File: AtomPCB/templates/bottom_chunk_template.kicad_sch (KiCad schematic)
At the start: 8 parts, among them J1 DF40HC_4.0_-40DS-0.4V_70_, U1 ATtiny416-M, U6 MPM3610AGQV-P

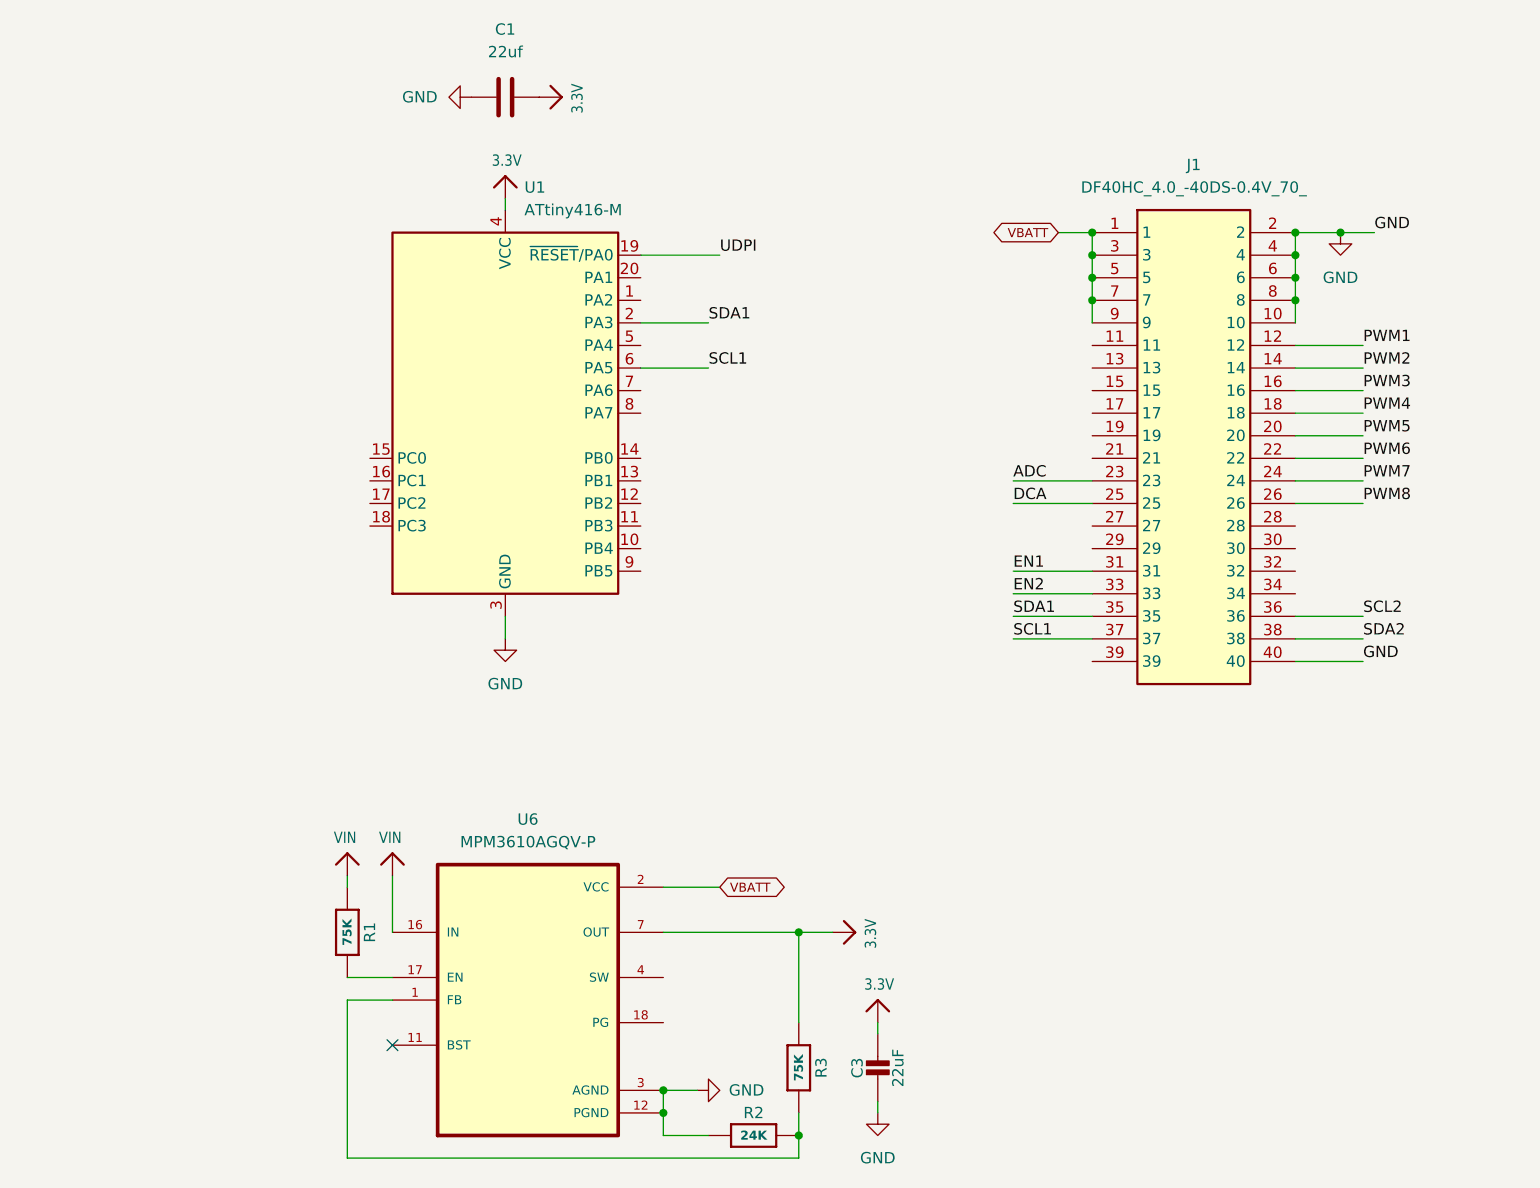
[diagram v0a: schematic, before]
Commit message: first pcb panel order placed!
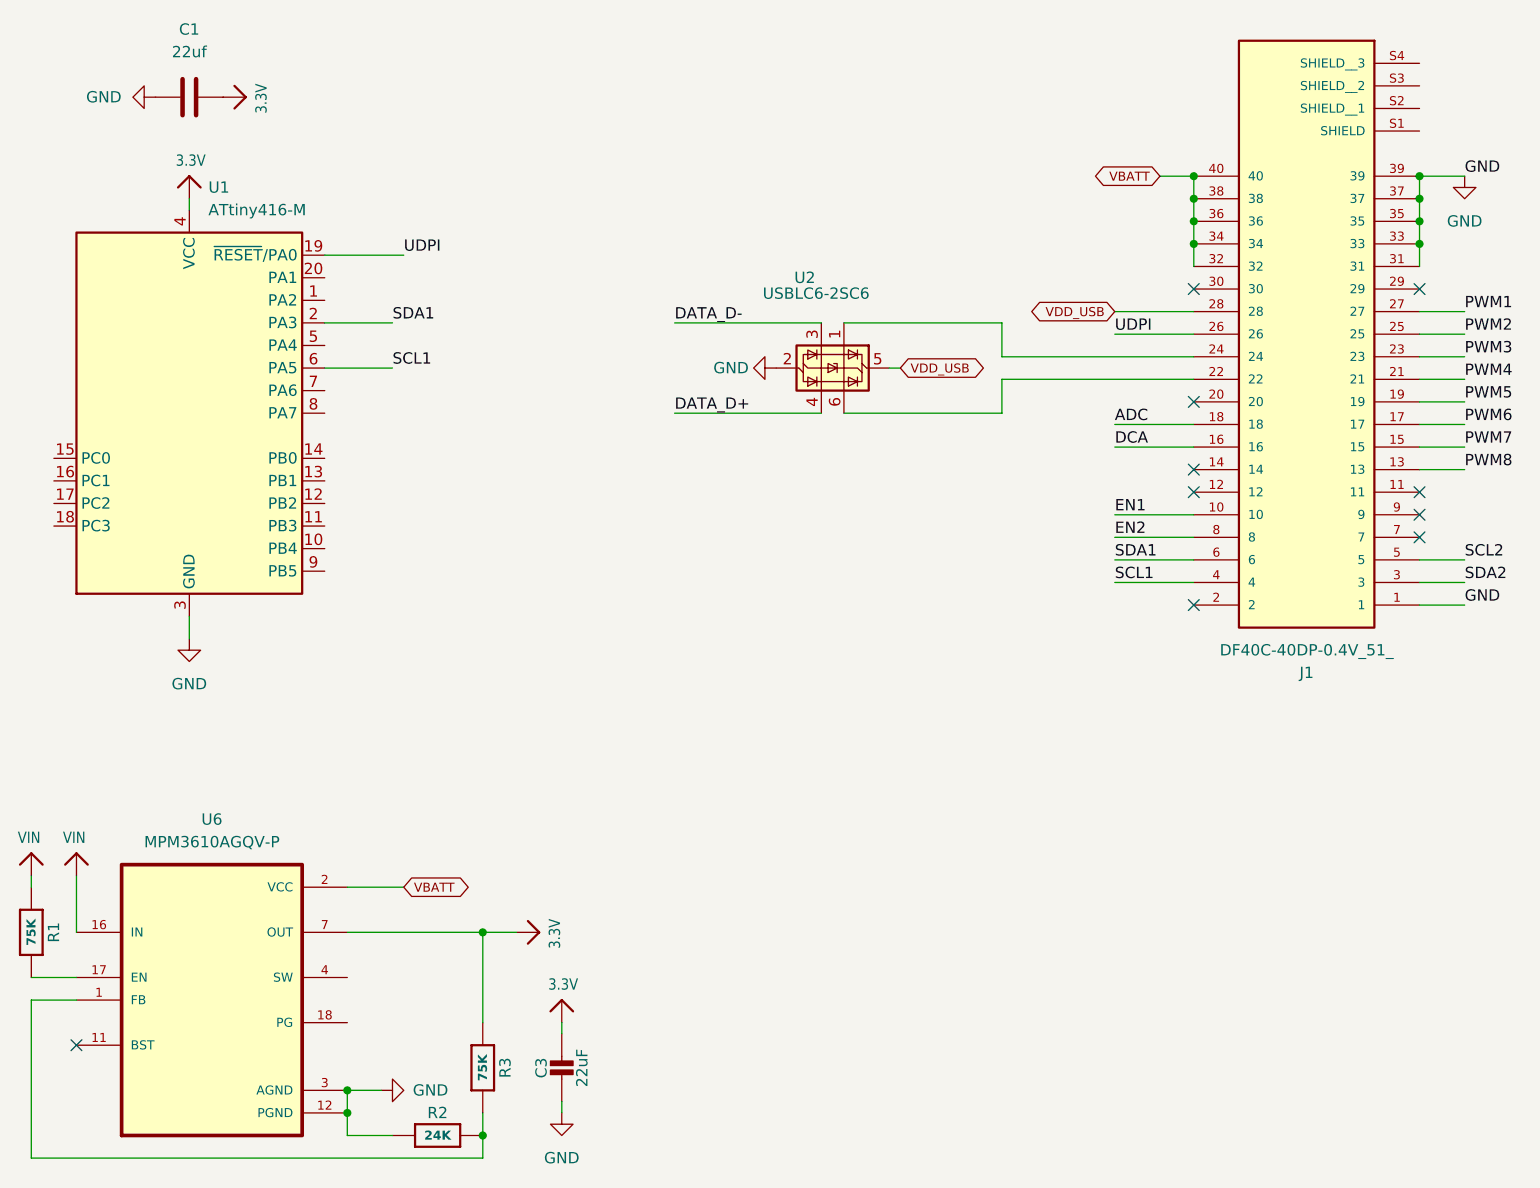
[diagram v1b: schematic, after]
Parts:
- removed J1: DF40HC_4.0_-40DS-0.4V_70_, HIROSE_DF40HC_40_connector:DF40HC4040DS04V70, symbol HIROSE_DF40HC_40_connector:DF40HC_4.0_-40DS-0.4V_70_
- added J1: DF40C-40DP-0.4V_51_, HIROSE_DF40C-40DP-0.4V_51_PLUG:HRS_DF40C-40DP-0.4V_51_, symbol DF40C40DP_0_4V_51:DF40C-40DP-0.4V_51_
- added U2: USBLC6-2SC6, Package_TO_SOT_SMD:SOT-23-6, symbol Power_Protection:USBLC6-2SC6
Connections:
- net ADC: now also J1.18
- net DCA: now also J1.16
- net EN1: now also J1.10
- net EN2: now also J1.8
- net GND: now also J1.1, J1.31, J1.33, J1.35, J1.37, J1.39, U2.2 (GND)
- net PWM1: now also J1.27
- net PWM2: now also J1.25
- net PWM3: now also J1.23
- net PWM4: now also J1.21
- net PWM5: now also J1.19
- net PWM6: now also J1.17
- net PWM7: now also J1.15
- net PWM8: now also J1.13
- net SCL1: now also J1.4
- net SCL2: now also J1.5
- net SDA1: now also J1.6
- net SDA2: now also J1.3
- net UDPI: now also J1.26
- net VBATT: now also J1.32, J1.34, J1.36, J1.38, J1.40
- new net: J1.22, U2.6 (I/O1)
- new net: J1.24, U2.1 (I/O1)
- new net DATA_D+: U2.4 (I/O2)
- new net DATA_D-: U2.3 (I/O2)
- new net VDD_USB: J1.28, U2.5 (VBUS)
- no-connect marks 1 -> 10
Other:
- moved on the sheet: C1, C3, R1, R2, R3, U1, U6
